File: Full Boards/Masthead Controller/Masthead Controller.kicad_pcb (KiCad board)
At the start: 4 copper layers, 80 x 150.1 mm, 169 parts, among them Q1 2N7002, Q2 2N7002, SW1 SW_MEC_5G, SW2 SW_MEC_5G

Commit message: Fixed reversed pin assignements on the Diodes Inc DMTH6010SK3Q.
Signed-off-by: digimer <digital.mermaid@gmail.com>
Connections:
- C10 pad 2: Net-(C10-Pad2) -> Net-(NFET1-D)
- C12 pad 2: Net-(C12-Pad2) -> Net-(NFET2-D)
- EF1 pad 1: Net-(C10-Pad2) -> Net-(NFET1-D)
- EF1 pad 2: Net-(C10-Pad2) -> Net-(NFET1-D)
- EF1 pad 3: Net-(C10-Pad2) -> Net-(NFET1-D)
- EF2 pad 1: Net-(C12-Pad2) -> Net-(NFET2-D)
- EF2 pad 2: Net-(C12-Pad2) -> Net-(NFET2-D)
- EF2 pad 3: Net-(C12-Pad2) -> Net-(NFET2-D)
- NFET1 pad 2: +24V_ISO -> Net-(NFET1-D)
- NFET1 pad 3: Net-(C10-Pad2) -> +24V_ISO
- NFET2 pad 2: +24V_ISO -> Net-(NFET2-D)
- NFET2 pad 3: Net-(C12-Pad2) -> +24V_ISO
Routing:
- net Net-(NFET2-D): track 0.00 -> 46.5 mm
- net Net-(C12-Pad2): track 39.3 -> 0.00 mm
- net Net-(C10-Pad2): track 33.9 -> 0.00 mm
- net Net-(NFET1-D): track 0.00 -> 30.3 mm
- net +24V_ISO: track 365.0 -> 338.6 mm, vias 12 -> 14
- net Net-(D2-K): track 25.7 -> 23.1 mm

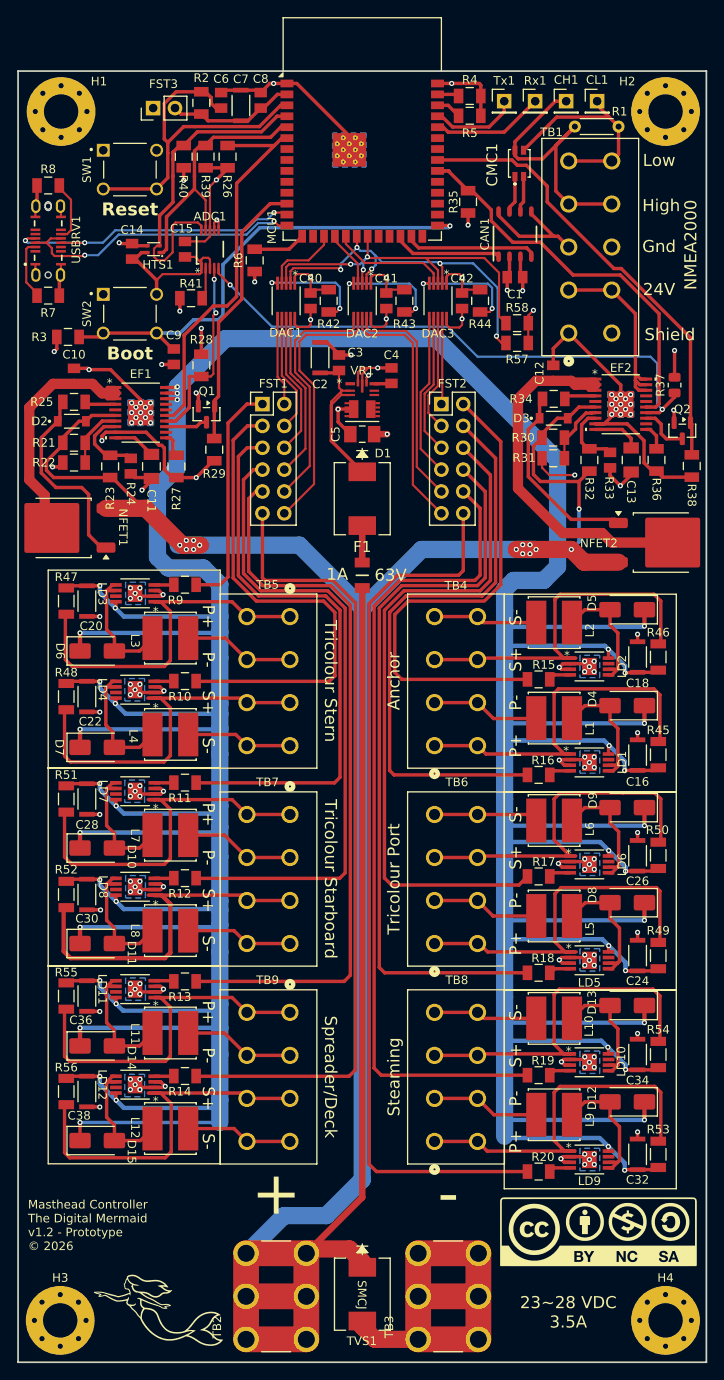
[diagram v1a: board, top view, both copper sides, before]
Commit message: Cleaned up vias and tracks.
Signed-off-by: digimer <digital.mermaid@gmail.com>
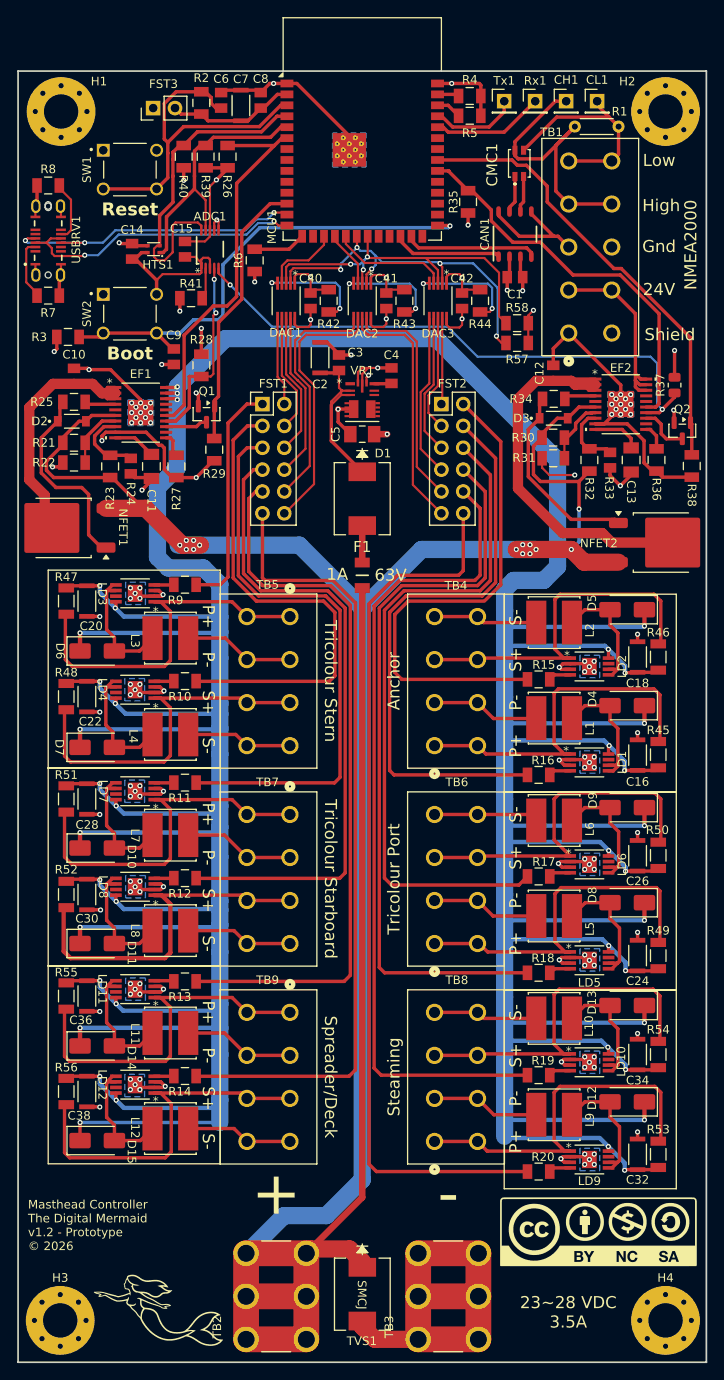
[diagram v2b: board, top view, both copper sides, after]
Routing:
- net GND: track 322.8 -> 307.5 mm
- net +24V_LED: track 701.3 -> 696.5 mm
- net +3.3V: track 59.4 -> 56.8 mm
- net Net-(LD4-ISENSE): track 43.0 -> 41.2 mm
- net Net-(D13-A): track 16.1 -> 14.3 mm
- net Net-(D15-A): track 15.9 -> 14.2 mm
- net Net-(D14-A): track 16.0 -> 14.3 mm
- net Net-(D11-A): track 16.0 -> 14.3 mm
- net Net-(D5-A): track 16.0 -> 14.3 mm
- net Net-(D10-A): track 16.0 -> 14.3 mm
- net +24V_ISO: track 338.6 -> 336.9 mm
- net /EFUSE_N2K_FAULT: track 46.4 -> 45.0 mm
- net Net-(LD6-ISENSE): track 42.0 -> 40.7 mm
- net Net-(LD2-ISENSE): track 42.5 -> 41.1 mm
- net Net-(LD10-ISENSE): track 43.0 -> 41.7 mm
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
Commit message: Updatedb the PCB with the new e-fuse config and added the +24V_ISO cap.
Signed-off-by: digimer <digital.mermaid@gmail.com>
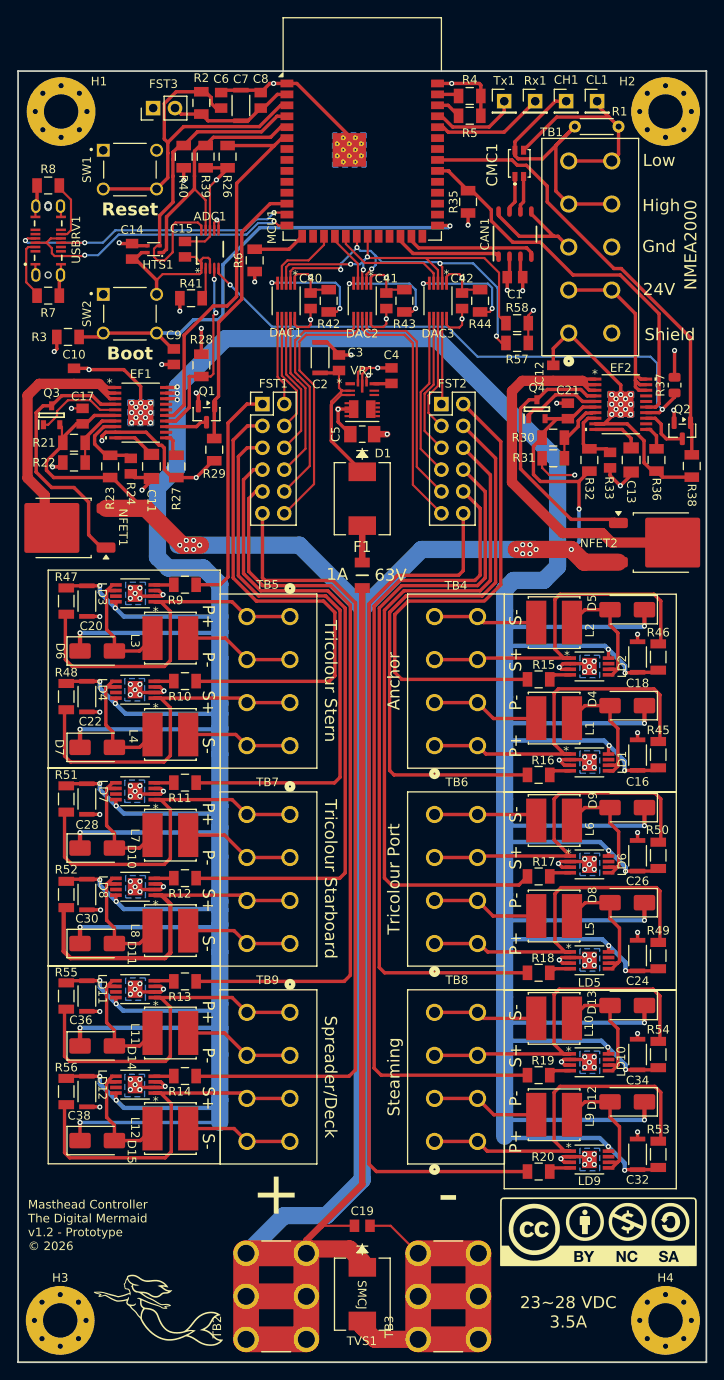
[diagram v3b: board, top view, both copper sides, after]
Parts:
- removed D2, D3: SZMMSZ52, mr-stuff:Onsemi SZMMSZ52
- removed R25, R34: 100kR, mr-stuff:Stackpole_RNCP1206
- added C17: 0.1μF, mr-stuff:Kyocera AVX 08051A0R8CAT2A, F.Cu at (67.5, 73.4)
- added C19: 1μF, mr-stuff:Kyocera AVX 08051A0R8CAT2A, F.Cu at (100.0, 167.5)
- added C21: 0.1μF, mr-stuff:Kyocera AVX 08051A0R8CAT2A, F.Cu at (123.9, 72.8)
- added Q3: BSS138P,215, mr-stuff:Nexperia BSS138P,215, F.Cu at (63.9, 73.3)
- added Q4: BSS138P,215, mr-stuff:Nexperia BSS138P,215, F.Cu at (120.3, 72.6)
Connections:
- EF1 pad 5: unconnected-(EF1-DRV-Pad5) -> Net-(EF1-DRV)
- EF2 pad 5: unconnected-(EF2-DRV-Pad5) -> Net-(EF2-DRV)
- NFET1 pad 1: Net-(D2-K) -> Net-(EF1-B_GATE)
- NFET2 pad 1: Net-(D3-K) -> Net-(EF2-B_GATE)
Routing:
- net Net-(EF2-B_GATE): track 3.20 -> 30.9 mm
- net Net-(EF1-B_GATE): track 3.23 -> 30.8 mm
- net Net-(D2-K): track 22.0 -> 0.00 mm
- net Net-(D3-K): track 21.9 -> 0.00 mm
- net GND: track 307.5 -> 317.9 mm, vias 133 -> 135
- net Net-(EF1-DRV): track 0.00 -> 10.3 mm
- net Net-(EF2-DRV): track 0.00 -> 9.48 mm
- net +24V_ISO: track 336.9 -> 345.7 mm
- net Net-(NFET1-D): track 29.2 -> 31.3 mm

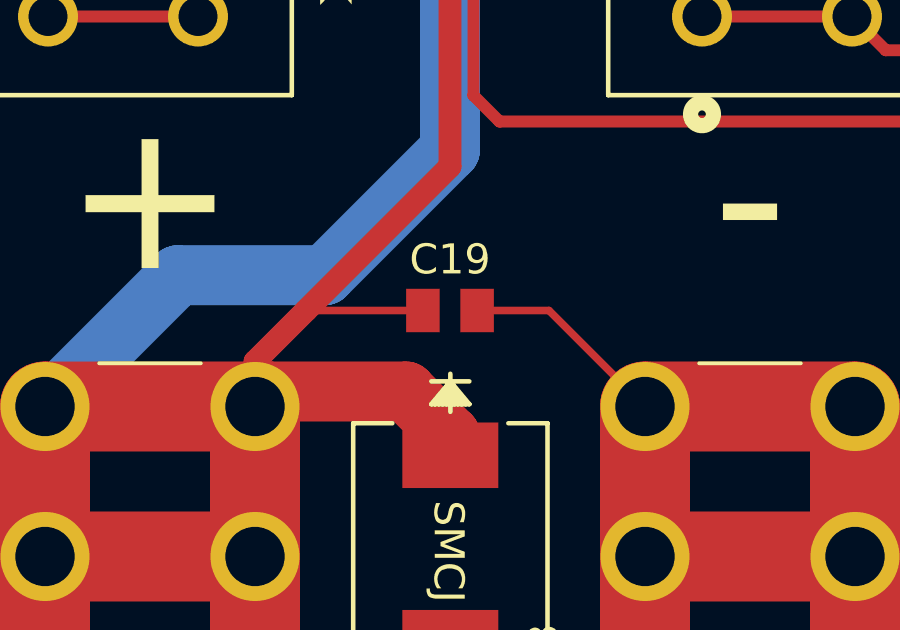
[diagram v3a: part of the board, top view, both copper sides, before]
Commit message: Added the new AVX 0805 generic footprint and updated the PCB to use it.
Signed-off-by: digimer <digital.mermaid@gmail.com>
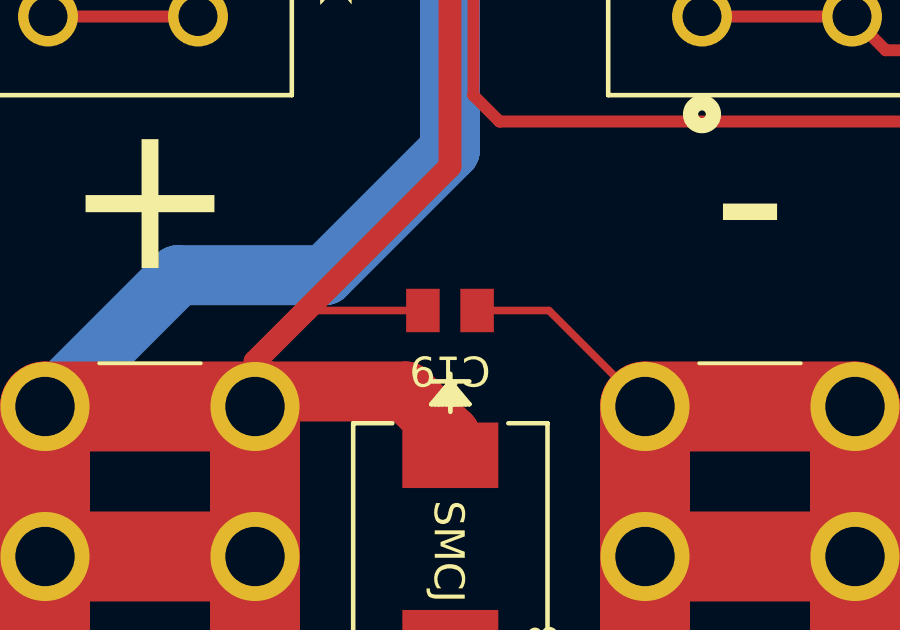
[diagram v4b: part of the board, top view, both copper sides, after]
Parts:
- C19: footprint mr-stuff:Kyocera AVX 08051A0R8CAT2A -> mr-stuff:Kyocera AVX 0805
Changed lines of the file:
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@@
 		)
 	)
-	(footprint "mr-stuff:Kyocera AVX 08051A0R8CAT2A"
+	(footprint "mr-stuff:Kyocera AVX 0805"
 		(layer "F.Cu")
 		(at 100 167.5 180)
 		(tags "08051C105K4Z2A ")
 		(property "Reference" "C19"
-			(at 0 1.7 0)
+			(at 0 -2 180)
 			(unlocked yes)
 			(layer "F.SilkS")
@@
 		)
 		(property "Datasheet" "https://mm.digikey.com/Volume0/opasdata/d220001/medias/docus/6397/AutoMLCC-2952695-DS.pdf"
-			(at 0 0 0)
+			(at 0 0 180)
 			(layer "F.Fab")
 			(hide yes)
@@
 		)
 		(property "Description" "Unpolarized capacitor"
-			(at 0 0 0)
+			(at 0 0 180)
 			(layer "F.Fab")
 			(hide yes)

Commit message: Changed EF2's ILIM from 90.9 kR to 28kR to get under the 30kR limit defined in the datasheet section 6.3.
Signed-off-by: digimer <digital.mermaid@gmail.com>
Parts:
- R36: value 90.9kR -> 28kR
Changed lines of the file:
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@@
 			)
 		)
-		(property "Value" "90.9kR"
+		(property "Value" "28kR"
 			(at 0 4.1 90)
 			(unlocked yes)
@@
 			)
 		)
-		(property "Description" "Resistor"
+		(property "Description" "28 kOhms ±1% 0.5W, 1/2W Chip Resistor 1206 (3216 Metric) Anti-Sulfur Thin Film"
 			(at 0 0 90)
 			(layer "F.Fab")
@@
 				)
 			)
+		)
+		(property "Part" "Stackpole RNCP1206FTD28K0"
+			(at 0 0 90)
+			(unlocked yes)
+			(layer "F.Fab")
+			(hide yes)
+			(effects
+				(font
+					(size 1 1)
+					(thickness 0.15)
+				)
+			)
